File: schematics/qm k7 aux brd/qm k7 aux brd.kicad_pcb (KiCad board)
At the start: 2 copper layers, 47 x 83.8 mm, 27 parts, among them J1 LEFT, J2 Micro_SD_Card, J3 Conn_01x03, J4 Conn_01x03, U1 AP1117-33, U2 CS4344-CZZ

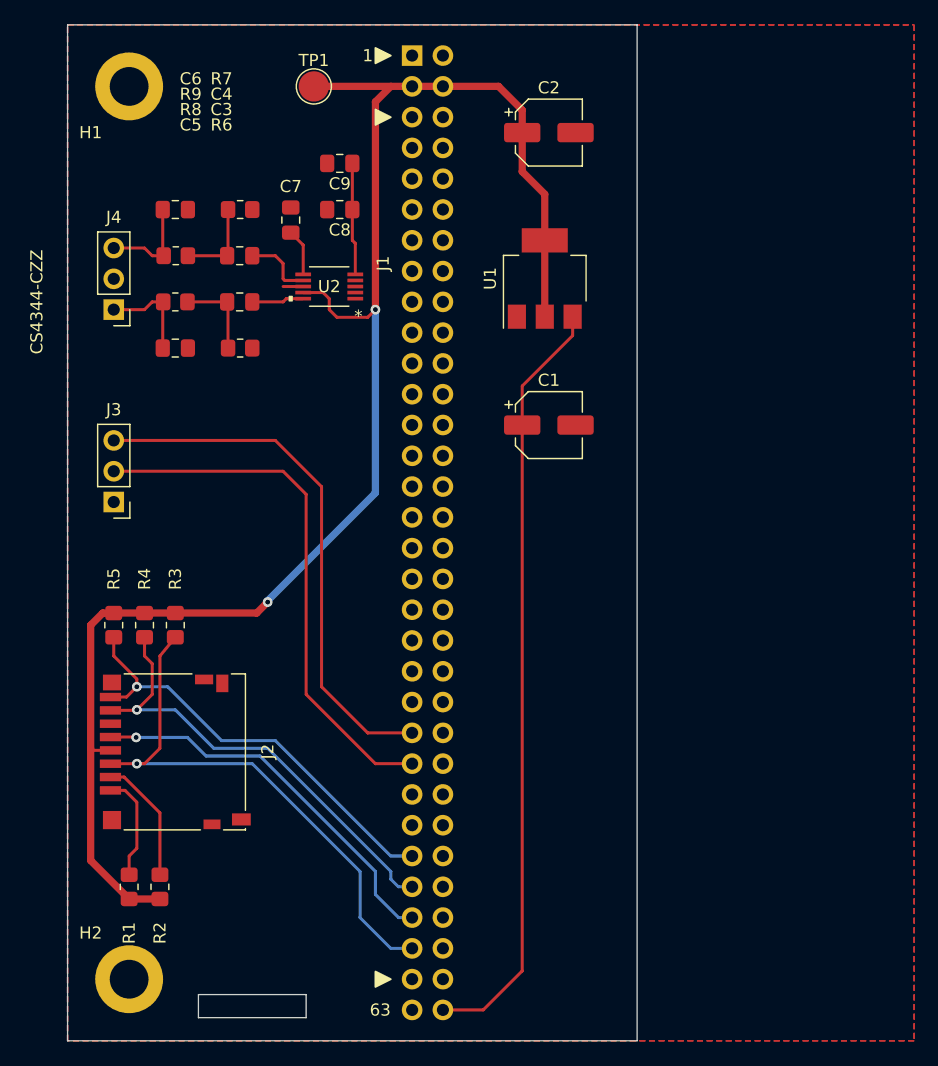
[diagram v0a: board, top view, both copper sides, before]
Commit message: Rv32: QM K7 aux schematic and STM32 breakout schematic. Both ordered.
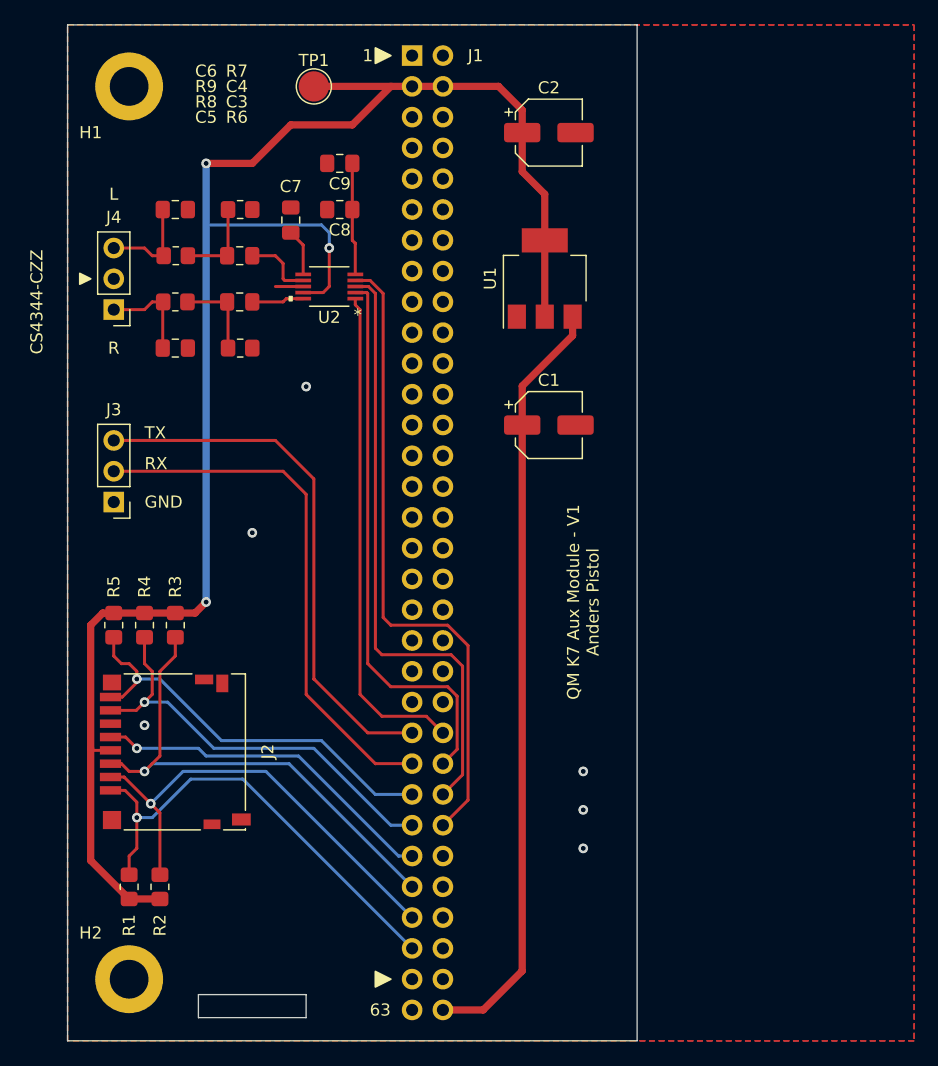
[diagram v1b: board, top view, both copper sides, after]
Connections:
- J1 pad 46: I2S_MCLK -> I2S_SDIN
- J1 pad 48: I2S_LRCK -> I2S_SCLK
- J1 pad 49: SD_DAT3 -> SD_DAT1
- J1 pad 50: I2S_SCLK -> I2S_LRCK
- J1 pad 51: SD_DAT2 -> SD_DAT0
- J1 pad 52: I2S_SDIN -> I2S_MCLK
- J1 pad 53: SD_DAT1 -> SD_CLK
- J1 pad 55: SD_DAT0 -> SD_CMD
- J1 pad 57: SD_CLK -> SD_DAT3
- J1 pad 59: SD_CMD -> SD_DAT2
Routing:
- net I2S_MCLK: track 0.00 -> 53.1 mm
- net I2S_LRCK: track 0.00 -> 50.2 mm
- net I2S_SCLK: track 0.00 -> 46.1 mm
- net I2S_SDIN: track 0.00 -> 41.0 mm
- net SD_DAT2: track 8.83 -> 38.6 mm, vias 0 -> 1
- net SD_DAT3: track 10.4 -> 38.1 mm, vias 0 -> 1
- net 3v3: track 135.9 -> 147.3 mm, vias 2 -> 3
- net SD_CMD: track 45.5 -> 41.7 mm
- net SD_CLK: track 32.2 -> 29.0 mm
- net SD_DAT0: track 38.2 -> 35.3 mm
- net SD_DAT1: track 35.9 -> 34.2 mm
- net GND: track 1.66 -> 2.30 mm, vias 0 -> 6
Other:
- board text added: "GND"
- board text added: "L"
- board text added: "QM K7 Aux Module - V1 Anders Pistol"
- board text added: "R"
- board text added: "RX"
- board text added: "TX"
